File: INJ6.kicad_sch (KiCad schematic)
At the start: 9 parts, among them U10 VNLD5160TR-E, U11 VNLD5160TR-E, U9 VNLD5160TR-E

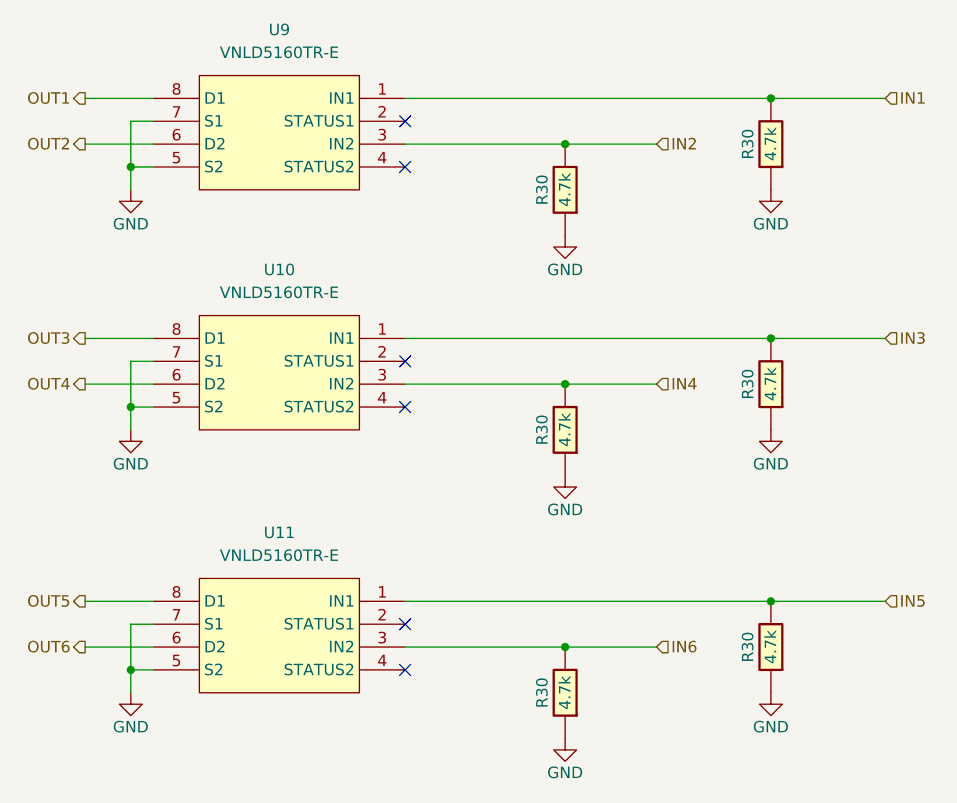
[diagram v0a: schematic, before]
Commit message: first changes from UAEFI to 4EFE ECU PCB dimensions
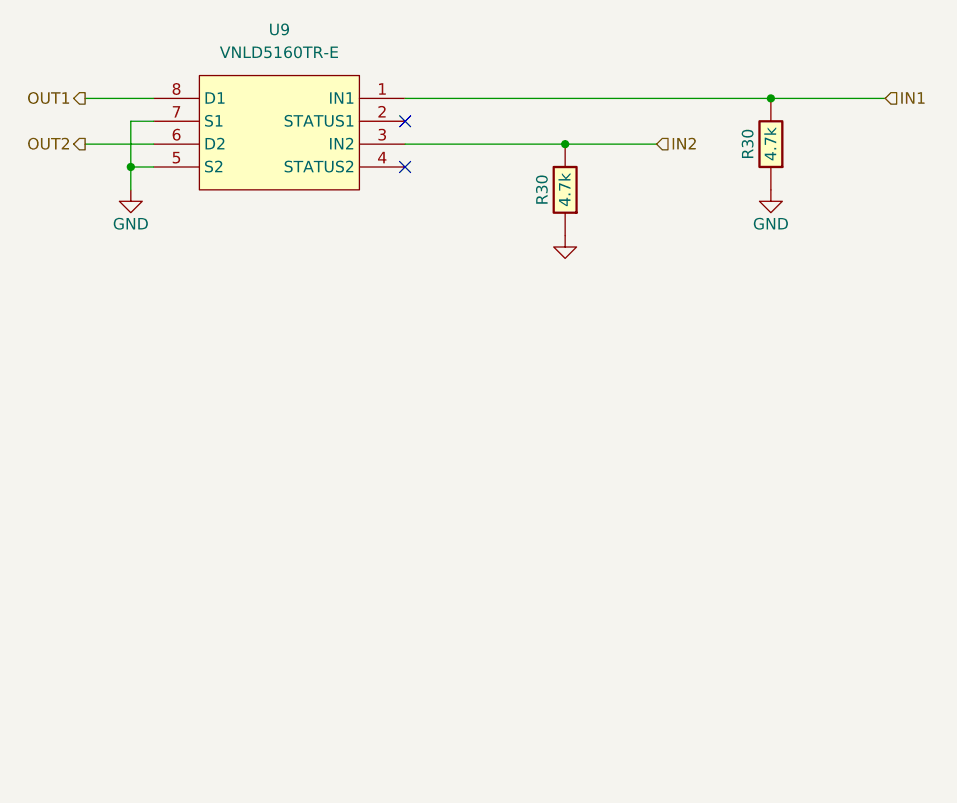
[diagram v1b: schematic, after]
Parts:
- removed R30 (x4): 4.7k, hellen-one-common:R0603, symbol hellen-one-common:Res
- removed U10, U11: VNLD5160TR-E, Package_SO:SOIC-8_3.9x4.9mm_P1.27mm, symbol chips:VNLD5160
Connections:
- no-connect marks 6 -> 2
